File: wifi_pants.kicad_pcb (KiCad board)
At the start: 2 copper layers, 65 x 30 mm, 62 parts, among them P1 CONN_02X20, P2 CONN_01X05, P3 CONN_01X02, U1 ESP-12E

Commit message: Layout switcher, clean up
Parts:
- removed JP7: EXT_5V, wifi_pants:GS2
- removed the REF** at (74.8, 85.8)
- removed the REF** at (100.0, 86.0)
- removed the REF** at (88.6, 107.8)
- added C2: 10uF X5R, mcous:1206(3216m)-CHIP-CAP, F.Cu at (97.1, 103.5)
- added C3: 100pF, mcous:0805(2012m)-CHIP-CAP, F.Cu at (94.8, 112.4)
- added C4: 10uF X5R, mcous:1206(3216m)-CHIP-CAP, F.Cu at (95.4, 107.0)
- added C5: 10uF X5R, mcous:1206(3216m)-CHIP-CAP, F.Cu at (92.9, 107.0)
- added JP1: Jumper_NO_Small, wifi_pants:GS2, B.Cu at (105.7, 113.5)
- added JP2: Jumper_NO_Small, wifi_pants:GS2, B.Cu at (110.8, 100.0)
- added L1: 2.2uH, wifi_pants:NR6028, F.Cu at (103.3, 107.3)
- added R7: 243K, mcous:0603(1608m)-CHIP-RESISTOR, F.Cu at (103.3, 111.7)
- added R8: 768K, mcous:0603(1608m)-CHIP-RESISTOR, F.Cu at (95.1, 110.4)
- added R9: 243K, mcous:0603(1608m)-CHIP-RESISTOR, F.Cu at (98.3, 110.4)
- added REF**: VIA_0.40mm, wifi_pants:VIA_0.40mm, F.Cu at (117.4, 93.1)
- added REF**: VIA_0.40mm, wifi_pants:VIA_0.40mm, F.Cu at (72.5, 111.1)
- added REF**: VIA_0.40mm, wifi_pants:VIA_0.40mm, F.Cu at (74.4, 109.4)
- added REF**: VIA_0.40mm, wifi_pants:VIA_0.40mm, F.Cu at (74.5, 95.0)
- added REF**: VIA_0.40mm, wifi_pants:VIA_0.40mm, F.Cu at (91.4, 110.4)
- added REF**: VIA_0.40mm, wifi_pants:VIA_0.40mm, F.Cu at (92.4, 114.2)
- added REF**: VIA_0.40mm, wifi_pants:VIA_0.40mm, F.Cu at (112.7, 104.4)
- added REF**: VIA_0.40mm, wifi_pants:VIA_0.40mm, F.Cu at (115.3, 104.4)
- added REF**: VIA_0.40mm, wifi_pants:VIA_0.40mm, F.Cu at (115.3, 100.9)
- added REF**: VIA_0.40mm, wifi_pants:VIA_0.40mm, F.Cu at (117.7, 100.9)
- added REF**: VIA_0.40mm, wifi_pants:VIA_0.40mm, F.Cu at (111.7, 98.5)
- added REF**: VIA_0.40mm, wifi_pants:VIA_0.40mm, F.Cu at (83.3, 93.8)
- added REF**: VIA_0.40mm, wifi_pants:VIA_0.40mm, F.Cu at (103.2, 95.6)
- added REF**: VIA_0.40mm, wifi_pants:VIA_0.40mm, F.Cu at (97.1, 102.0)
- added REF**: VIA_0.40mm, wifi_pants:VIA_0.40mm, F.Cu at (101.4, 102.0)
- added REF**: VIA_0.40mm, wifi_pants:VIA_0.40mm, F.Cu at (110.0, 114.2)
- added REF**: VIA_0.40mm, wifi_pants:VIA_0.40mm, F.Cu at (97.2, 114.2)
- added REF**: VIA_0.40mm, wifi_pants:VIA_0.40mm, F.Cu at (99.4, 111.8)
- added REF**: VIA_0.40mm, wifi_pants:VIA_0.40mm, F.Cu at (97.2, 111.8)
- added REF**: VIA_0.40mm, wifi_pants:VIA_0.40mm, F.Cu at (97.1, 105.9)
- added REF**: VIA_0.40mm, wifi_pants:VIA_0.40mm, F.Cu at (99.0, 105.6)
- added REF**: VIA_0.40mm, wifi_pants:VIA_0.40mm, F.Cu at (97.1, 104.8)
- added REF**: VIA_0.40mm, wifi_pants:VIA_0.40mm, F.Cu at (84.1, 95.9)
- added REF**: VIA_0.40mm, wifi_pants:VIA_0.40mm, F.Cu at (94.1, 104.2)
- added REF**: VIA_0.40mm, wifi_pants:VIA_0.40mm, F.Cu at (89.5, 104.3)
- added REF**: VIA_0.40mm, wifi_pants:VIA_0.40mm, F.Cu at (113.8, 114.2)
- added REF**: VIA_0.40mm, wifi_pants:VIA_0.40mm, F.Cu at (80.0, 109.6)
- added REF**: VIA_0.40mm, wifi_pants:VIA_0.40mm, F.Cu at (87.3, 91.5)
- added REF**: VIA_0.40mm, wifi_pants:VIA_0.40mm, F.Cu at (76.1, 98.1)
- added REF**: VIA_0.40mm, wifi_pants:VIA_0.40mm, F.Cu at (74.4, 99.7)
- added REF**: VIA_0.40mm, wifi_pants:VIA_0.40mm, F.Cu at (73.6, 105.3)
- added REF**101: VIA_0.40mm, wifi_pants:VIA_0.40mm, F.Cu at (123.6, 85.8)
- added REF**101: VIA_0.40mm, wifi_pants:VIA_0.40mm, F.Cu at (120.3, 85.8)
- added REF**11: VIA_0.40mm, wifi_pants:VIA_0.40mm, F.Cu at (74.6, 85.8)
- added REF**1112: VIA_0.40mm, wifi_pants:VIA_0.40mm, F.Cu at (65.8, 103.0)
- added REF**1113: VIA_0.40mm, wifi_pants:VIA_0.40mm, F.Cu at (65.8, 106.0)
- added REF**112: VIA_0.40mm, wifi_pants:VIA_0.40mm, F.Cu at (65.8, 97.0)
- added REF**113: VIA_0.40mm, wifi_pants:VIA_0.40mm, F.Cu at (65.8, 94.0)
- added REF**21: VIA_0.40mm, wifi_pants:VIA_0.40mm, F.Cu at (79.7, 85.8)
- added REF**31: VIA_0.40mm, wifi_pants:VIA_0.40mm, F.Cu at (84.8, 85.8)
- added REF**41: VIA_0.40mm, wifi_pants:VIA_0.40mm, F.Cu at (89.8, 85.8)
- added REF**51: VIA_0.40mm, wifi_pants:VIA_0.40mm, F.Cu at (94.9, 85.8)
- added REF**61: VIA_0.40mm, wifi_pants:VIA_0.40mm, F.Cu at (100.0, 85.8)
- added REF**71: VIA_0.40mm, wifi_pants:VIA_0.40mm, F.Cu at (105.1, 85.8)
- added REF**81: VIA_0.40mm, wifi_pants:VIA_0.40mm, F.Cu at (110.2, 85.8)
- added REF**91: VIA_0.40mm, wifi_pants:VIA_0.40mm, F.Cu at (115.2, 85.8)
- added U2: TPS61252, wifi_pants:WSON-8-1EP_2x2mm_Pitch0.5mm, F.Cu at (98.6, 107.8)
- P2: value CONN_01X05 -> POWER / UART
- P3: value CONN_01X02 -> JST PH POWER IN
- R1, R2, R3, R4, R5, R6: value 150 -> 33
- moved REF**1111 3.63 mm to (65.8, 100.0)
- moved REF** 3.15 mm to (129.2, 100.0)
- moved REF** 1.68 mm to (91.2, 106.3)
- moved REF** 0.48 mm to (85.1, 97.2)
- moved REF** 0.46 mm to (100.0, 91.5)
- moved REF** 0.40 mm to (105.3, 91.9)
- moved REF** 0.05 mm to (85.1, 99.6)
- renumbered JP6 to JP3, REF** to REF**1111
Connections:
- P2 pad 2: PSU_EN -> /PSU_SHDN
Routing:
- net PWR_IN: track 0.00 -> 45.7 mm, vias 0 -> 1
- net /PSU_SHDN: track 0.00 -> 25.7 mm, vias 0 -> 2
- net PI_UART0_RXD: track 66.9 -> 92.2 mm
- net +5V: track 36.5 -> 59.7 mm, vias 2 -> 3
- net PI_UART0_TXD: track 68.1 -> 87.3 mm
- net Net-(C3-Pad2): track 0.00 -> 7.04 mm
- net ID_SD: track 53.9 -> 52.7 mm
- added copper zone on F.Cu, net +5V
- added copper zone on F.Cu, net Net-(L1-Pad2)
- added copper zone on F.Cu, net PWR_IN
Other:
- net class 5V added: clearance 0.2, trace_width 0.8, via_dia 1, via_drill 0.6

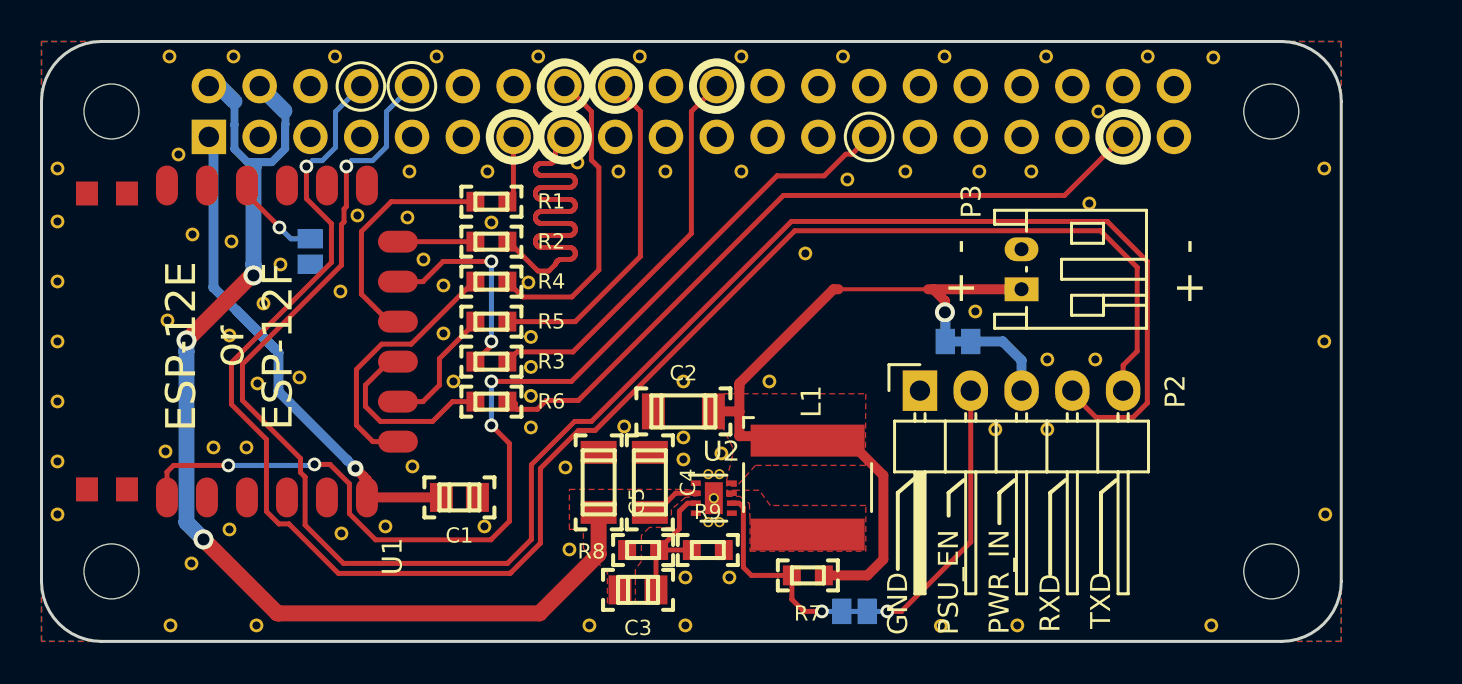
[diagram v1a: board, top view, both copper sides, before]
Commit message: Changed to a different switcher
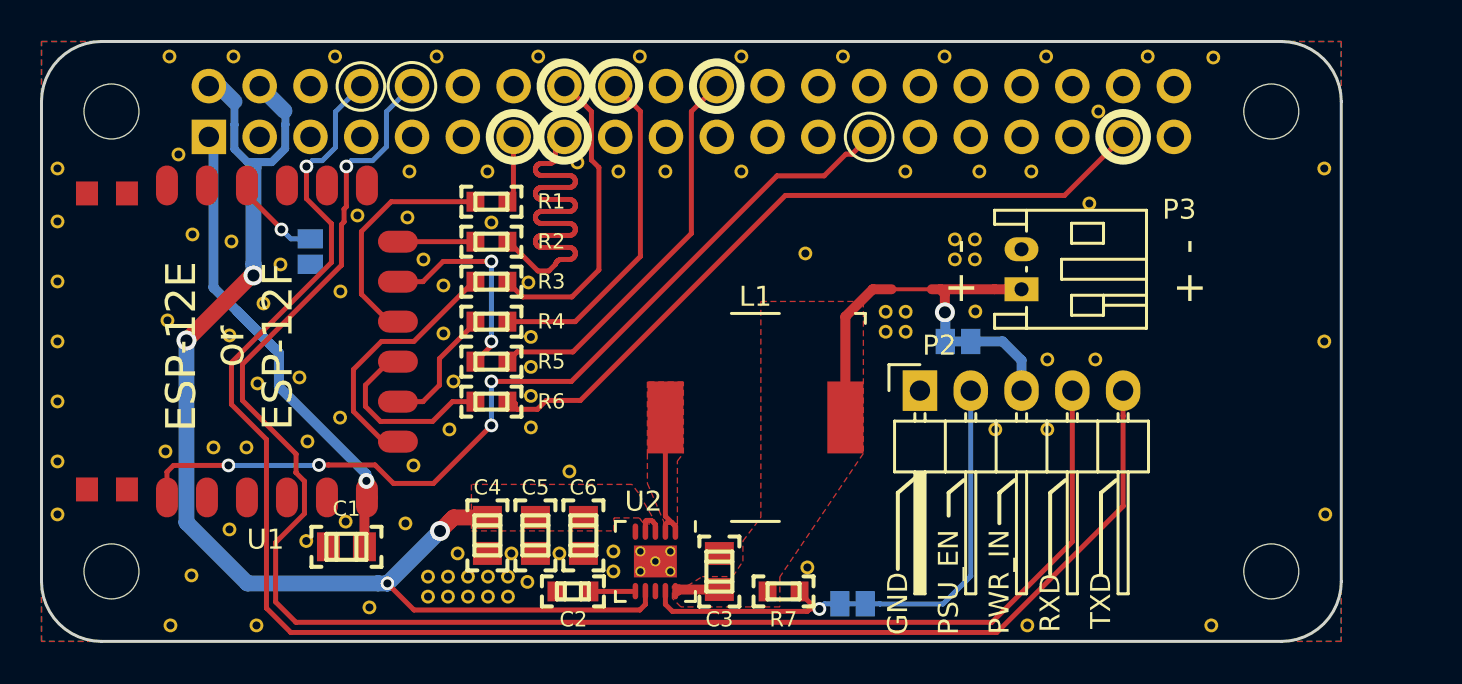
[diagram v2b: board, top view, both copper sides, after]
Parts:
- removed R8: 768K, mcous:0603(1608m)-CHIP-RESISTOR
- removed R9: 243K, mcous:0603(1608m)-CHIP-RESISTOR
- removed the REF** at (91.4, 110.4)
- removed the REF** at (92.4, 114.2)
- removed the REF** at (97.1, 102.0)
- removed the REF** at (101.4, 102.0)
- removed the REF** at (110.0, 114.2)
- removed the REF** at (97.2, 114.2)
- removed the REF** at (99.4, 111.8)
- removed the REF** at (97.2, 111.8)
- removed the REF** at (97.1, 105.9)
- removed the REF** at (99.0, 105.6)
- removed the REF** at (97.1, 104.8)
- removed the REF** at (94.1, 104.2)
- removed the REF** at (113.8, 114.2)
- removed the REF** at (80.0, 109.6)
- removed the REF** at (82.2, 109.2)
- added C6: 10uF X5R, mcous:0805(2012m)-CHIP-CAP, F.Cu at (92.1, 109.7)
- added REF**: VIA_0.40mm, wifi_pants:VIA_0.40mm, F.Cu at (78.3, 105.0)
- added REF**: VIA_0.40mm, wifi_pants:VIA_0.40mm, F.Cu at (79.9, 103.8)
- added REF**1: VIA_0.40mm, wifi_pants:VIA_0.40mm, F.Cu at (114.3, 114.2)
- added REF**1: VIA_0.40mm, wifi_pants:VIA_0.40mm, F.Cu at (81.4, 113.3)
- added REF**1: VIA_0.40mm, wifi_pants:VIA_0.40mm, F.Cu at (110.7, 94.9)
- added REF**1: VIA_0.40mm, wifi_pants:VIA_0.40mm, F.Cu at (107.2, 98.5)
- added REF**1: VIA_0.40mm, wifi_pants:VIA_0.40mm, F.Cu at (84.3, 111.8)
- added REF**10: VIA_0.40mm, wifi_pants:VIA_0.40mm, F.Cu at (84.3, 112.8)
- added REF**2: VIA_0.40mm, wifi_pants:VIA_0.40mm, F.Cu at (85.3, 111.8)
- added REF**2: VIA_0.40mm, wifi_pants:VIA_0.40mm, F.Cu at (111.7, 94.9)
- added REF**2: VIA_0.40mm, wifi_pants:VIA_0.40mm, F.Cu at (108.2, 98.5)
- added REF**3: VIA_0.40mm, wifi_pants:VIA_0.40mm, F.Cu at (86.3, 111.8)
- added REF**3: VIA_0.40mm, wifi_pants:VIA_0.40mm, F.Cu at (93.6, 110.5)
- added REF**3: VIA_0.40mm, wifi_pants:VIA_0.40mm, F.Cu at (89.3, 112.0)
- added REF**4: VIA_0.40mm, wifi_pants:VIA_0.40mm, F.Cu at (87.3, 111.8)
- added REF**4: VIA_0.40mm, wifi_pants:VIA_0.40mm, F.Cu at (90.9, 110.6)
- added REF**4: VIA_0.40mm, wifi_pants:VIA_0.40mm, F.Cu at (88.5, 110.6)
- added REF**4: VIA_0.40mm, wifi_pants:VIA_0.40mm, F.Cu at (85.8, 110.6)
- added REF**4: VIA_0.40mm, wifi_pants:VIA_0.40mm, F.Cu at (93.6, 111.5)
- added REF**5: VIA_0.40mm, wifi_pants:VIA_0.40mm, F.Cu at (88.3, 111.8)
- added REF**5: VIA_0.40mm, wifi_pants:VIA_0.40mm, F.Cu at (111.7, 95.9)
- added REF**5: VIA_0.40mm, wifi_pants:VIA_0.40mm, F.Cu at (108.2, 99.5)
- added REF**6: VIA_0.40mm, wifi_pants:VIA_0.40mm, F.Cu at (88.3, 112.8)
- added REF**6: VIA_0.40mm, wifi_pants:VIA_0.40mm, F.Cu at (78.2, 110.0)
- added REF**6: VIA_0.40mm, wifi_pants:VIA_0.40mm, F.Cu at (80.2, 109.0)
- added REF**6: VIA_0.40mm, wifi_pants:VIA_0.40mm, F.Cu at (110.7, 95.9)
- added REF**6: VIA_0.40mm, wifi_pants:VIA_0.40mm, F.Cu at (107.2, 99.5)
- added REF**6: VIA_0.40mm, wifi_pants:VIA_0.40mm, F.Cu at (103.3, 111.3)
- added REF**7: VIA_0.40mm, wifi_pants:VIA_0.40mm, F.Cu at (87.3, 112.8)
- added REF**8: VIA_0.40mm, wifi_pants:VIA_0.40mm, F.Cu at (86.3, 112.8)
- added REF**9: VIA_0.40mm, wifi_pants:VIA_0.40mm, F.Cu at (85.3, 112.8)
- C2: value 10uF X5R -> 0.15uF X5R; footprint mcous:1206(3216m)-CHIP-CAP -> mcous:0603(1608m)-CHIP-CAP
- C3: value 100pF -> 22uF X5R
- C4, C5: footprint mcous:1206(3216m)-CHIP-CAP -> mcous:0805(2012m)-CHIP-CAP
- L1: value 2.2uH -> 1.0uH; footprint wifi_pants:NR6028 -> wifi_pants:SRU1028-1R
- R7: value 243K -> 47K
- U2: value TPS61252 -> TPS6123x; footprint wifi_pants:WSON-8-1EP_2x2mm_Pitch0.5mm -> wifi_pants:VSON-10
- moved REF** 28.0 mm to (83.2, 109.1)
- moved C2 10.6 mm to (91.6, 112.5)
- moved C4 8.55 mm to (87.3, 109.7), turned to 270 degrees
- moved C1 6.17 mm to (80.2, 110.3), turned to 180 degrees
- moved REF** 5.16 mm to (85.4, 104.4)
- moved L1 4.37 mm to (100.7, 103.8), turned to 180 degrees
- moved U2 4.31 mm to (95.7, 111.0), turned to 180 degrees
- moved C3 4.17 mm to (98.9, 111.5), turned to 90 degrees
- moved C5 4.13 mm to (89.7, 109.7), turned to 270 degrees
- moved R7 1.46 mm to (102.1, 112.5)
- moved REF** 0.60 mm to (72.5, 111.7)
- moved JP1 0.39 mm to (105.6, 113.1), turned to 90 degrees
- moved REF** 0.28 mm to (91.4, 106.5)
- moved REF** 0.07 mm to (83.6, 106.2)
- renumbered R4 to R3, R5 to R4, R3 to R5
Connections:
- C2 pad 1: PWR_IN -> Net-(C2-Pad1)
- C3 pad 1: +5V -> PWR_IN
- C3 pad 2: Net-(C3-Pad2) -> GND
- R7 pad 1: /PSU_SHDN -> PWR_IN
- R7 pad 2: PWR_IN -> /PSU_SHDN
- U2 pad 1: GND -> Net-(L1-Pad2)
- U2 pad 2: +5V -> Net-(L1-Pad2)
- U2 pad 3: Net-(C3-Pad2) -> +5V
- U2 pad 4: GND -> +5V
- U2 pad 6: /PSU_SHDN -> Net-(C2-Pad1)
- U2 pad 7: Net-(L1-Pad2) -> +5V
- U2 pad 8: PWR_IN -> Net-(U2-Pad8)
- U2 pad 9: GND -> /PSU_SHDN
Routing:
- net PWR_IN: track 45.7 -> 25.0 mm
- net PI_UART0_RXD: track 92.2 -> 81.3 mm
- net ID_SD: track 52.7 -> 45.4 mm
- net Net-(C3-Pad2): track 7.04 -> 0.00 mm
- net Net-(L1-Pad2): track 0.00 -> 6.91 mm
- net PI_UART0_TXD: track 87.3 -> 82.6 mm
- net +5V: track 59.7 -> 63.3 mm, vias 3 -> 4
- net Net-(C2-Pad1): track 0.00 -> 2.33 mm
- net /PSU_SHDN: track 25.7 -> 27.8 mm, vias 2 -> 1
- net +3V3: track 27.6 -> 26.7 mm

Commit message: Clean up PSU layout and silk
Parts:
- removed the REF** at (112.7, 104.4)
- removed the REF** at (115.3, 104.4)
- removed the REF** at (77.9, 101.8)
- removed the REF**1 at (84.3, 111.8)
- removed REF**10: VIA_0.40mm, wifi_pants:VIA_0.40mm
- added REF**: Fiducial_1mm_Dia_2.54mm_Outer_CopperTop, Fiducials:Fiducial_1mm_Dia_2.54mm_Outer_CopperTop, F.Cu at (128.0, 93.5)
- added REF**: VIA_0.40mm, wifi_pants:VIA_0.40mm, F.Cu at (96.4, 99.8)
- added REF**: VIA_0.40mm, wifi_pants:VIA_0.40mm, F.Cu at (95.0, 101.2)
- added REF**: VIA_0.40mm, wifi_pants:VIA_0.40mm, F.Cu at (93.6, 102.6)
- added REF**: Fiducial_1mm_Dia_2.54mm_Outer_CopperTop, Fiducials:Fiducial_1mm_Dia_2.54mm_Outer_CopperTop, F.Cu at (73.7, 113.0)
- added REF**1: VIA_0.40mm, wifi_pants:VIA_0.40mm, F.Cu at (103.3, 113.3)
- added REF**1: VIA_0.40mm, wifi_pants:VIA_0.40mm, F.Cu at (84.0, 113.2)
- added REF**1: VIA_0.40mm, wifi_pants:VIA_0.40mm, F.Cu at (93.6, 113.0)
- added REF**6: VIA_0.40mm, wifi_pants:VIA_0.40mm, F.Cu at (107.1, 105.7)
- added REF**6: VIA_0.40mm, wifi_pants:VIA_0.40mm, F.Cu at (105.1, 108.1)
- C1: value 10uF -> 10uF X5R
- JP1: value Jumper_NO_Small -> /PSU_SHDN ISOL
- JP2: value Jumper_NO_Small -> PWR_IN ISOL
- moved REF**3 5.14 mm to (93.6, 109.2)
- moved REF** 2.30 mm to (93.6, 105.8)
- moved REF**1 2.07 mm to (79.3, 113.2)
- moved JP1 2.00 mm to (105.6, 111.1)
- moved REF**1 1.78 mm to (108.9, 94.9)
- moved REF**2 1.78 mm to (109.9, 94.9)
- moved REF**5 1.78 mm to (109.9, 95.9)
- moved REF**6 1.78 mm to (108.9, 95.9)
- moved REF** 1.69 mm to (78.7, 102.6)
- moved REF**2 1.36 mm to (86.4, 111.0)
- moved REF**3 1.36 mm to (87.4, 111.0)
- moved REF**4 1.36 mm to (88.4, 111.0)
- moved REF**5 1.36 mm to (89.4, 111.0)
- moved REF**6 1.36 mm to (89.4, 112.0)
- moved REF**7 1.36 mm to (88.4, 112.0)
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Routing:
- net PWR_IN: track 25.0 -> 37.7 mm
- net +5V: track 63.3 -> 71.7 mm, vias 4 -> 3
- net PI_UART0_RXD: track 81.3 -> 75.8 mm
- net GND: track 0.66 -> 3.36 mm
- net /PSU_SHDN: track 27.8 -> 25.5 mm
- net Net-(L1-Pad2): track 6.91 -> 5.89 mm
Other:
- rule trace_min: 0.1524 -> 0.006
- rule via_min_size: 0.6858 -> 0.027
- board text added: "/PWR_SHDN isolation"
- board text added: "/SHDN"
- board text added: "ESP GPIO0 25MHz SDIO"
- board text added: "PWR_IN isolation"
- board text added: "r3"
- board text removed: "PSU_EN"
- board text removed: "r3b0"
